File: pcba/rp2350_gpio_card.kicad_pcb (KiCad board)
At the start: 2 copper layers, 26 x 30 mm, 41 parts, among them J1 Conn_01x10_Pin, J2 Conn_01x10_Pin, P1 USB_C_Plug_USB2.0, U1 RP2350_60QFN, U2 W25Q128JVS, U4 AP2127K-3.3, Y1 ABM8-272-T3

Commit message: add copyright claim
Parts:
- moved C1 3.78 mm to (92.7, 65.0)
- moved C13 3.78 mm to (112.5, 75.7)
- moved C15 3.78 mm to (114.2, 58.0)
- moved C3 3.78 mm to (95.3, 64.5)
- moved R4 3.78 mm to (99.7, 57.5)
- moved R6 3.78 mm to (102.0, 72.5)
- moved R8 3.78 mm to (112.5, 64.9)
- moved Y1 3.78 mm to (113.1, 61.6)
- moved C10 3.78 mm to (108.6, 61.6)
- moved C12 3.78 mm to (114.1, 68.0)
- moved C14 3.78 mm to (103.6, 60.0)
- moved C16 3.78 mm to (113.9, 64.0)
- moved C17 3.78 mm to (97.8, 66.1)
- moved C19 3.78 mm to (94.1, 54.1)
- moved C2 3.78 mm to (110.8, 56.7)
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
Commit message: update design
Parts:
- J1, J2: footprint Connector_Harwin:Harwin_M20-89010xx_1x10_P2.54mm_Horizontal -> RP2350CardCustomFootprintsLibrary:Custom_Harwin_M20-89010xx_1x10_P2.54mm_Horizontal
- moved REF** 11.4 mm to (112.6, 56.0)
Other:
- board text added: "EE student at Polytechnic University of Turin"

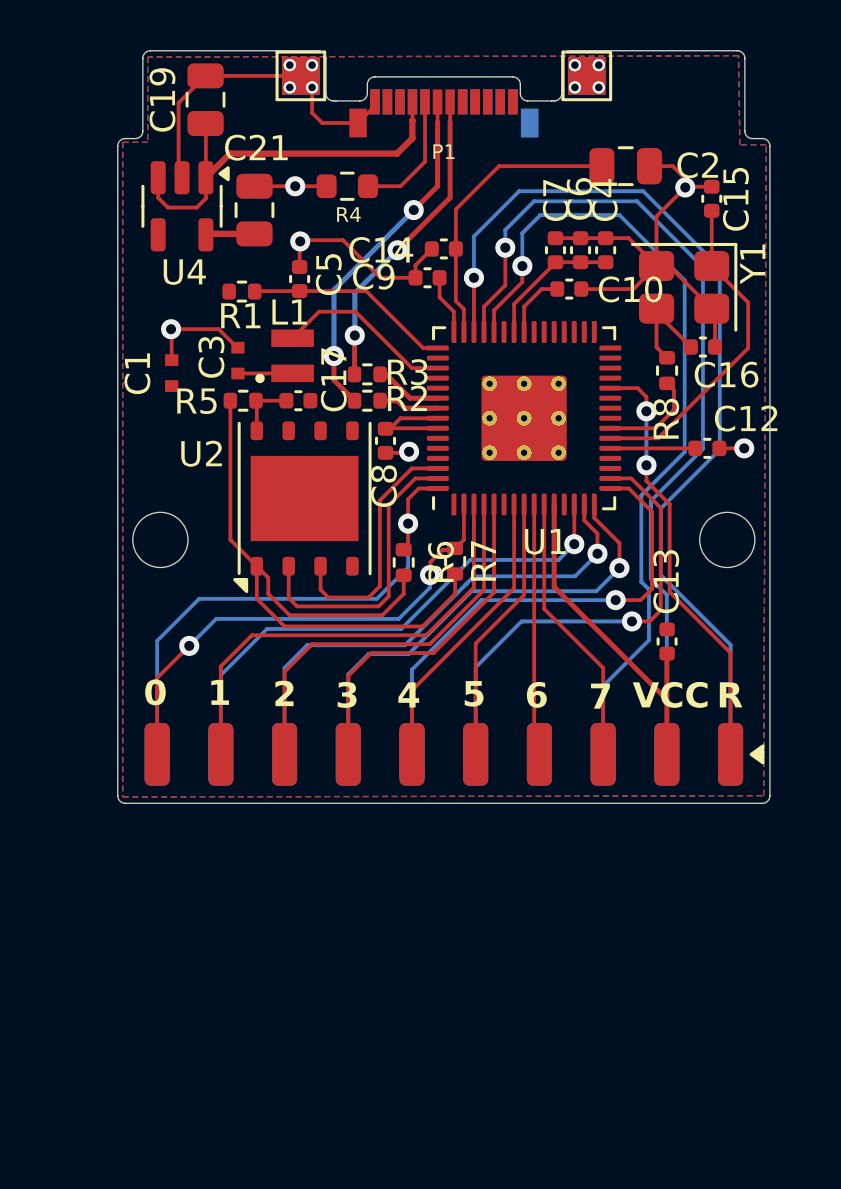
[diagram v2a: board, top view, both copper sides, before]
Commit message: version 1.2.4 - fix floating pads and some errors
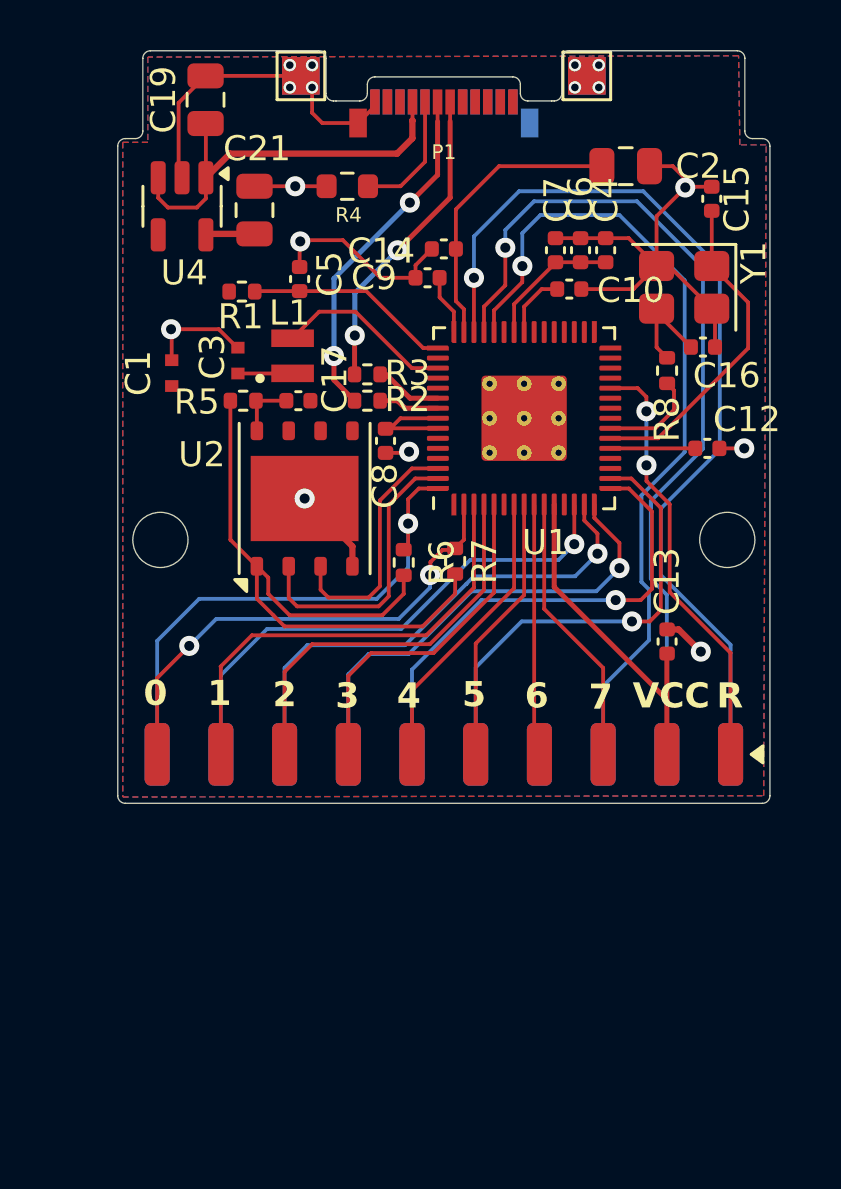
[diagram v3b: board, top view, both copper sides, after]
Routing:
- net GND: track 48.2 -> 53.4 mm, vias 14 -> 16
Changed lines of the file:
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@@
 	(paper "A5")
 	(title_block
-		(title "RP2350 GPIO Card V1.2.2")
+		(title "RP2350 GPIO Card V1.2.4")
 		(date "2025-08-07")
 		(rev "X1")
@@
 	)
 	(segment
-		(start 103.305183 57.546434)
+		(start 103.305183 57.094817)
 		(end 103.305183 54.971434)
 		(width 0.2)
@@
 	)
 	(segment
-		(start 102.355183 58.496434)
-		(end 103.305183 57.546434)
+		(start 102.2 58.2)
+		(end 103.305183 57.094817)
 		(width 0.2)
 		(layer "F.Cu")
@@
 	)
 	(via
-		(at 102.355183 58.496434)
+		(at 102.2 58.2)
 		(size 0.8)
 		(drill 0.4)
@@
 	)
 	(segment
-		(start 99.174254 61.677363)
-		(end 102.355183 58.496434)
+		(start 99.174254 61.225746)
+		(end 99.174254 64.31513)
 		(width 0.2)
 		(layer "B.Cu")
@@
 	)
 	(segment
-		(start 99.174254 64.31513)
-		(end 99.174254 61.677363)
+		(start 102.2 58.2)
+		(end 99.174254 61.225746)
 		(width 0.2)
 		(layer "B.Cu")
@@
 	)
 	(segment
+		(start 99.910183 72.696434)
+		(end 99.910183 71.901434)
+		(width 0.25)
+		(layer "F.Cu")
+		(net 55)
+	)
+	(segment
 		(start 95.315183 63.981434)
 		(end 94.580183 63.246434)
@@
 	)
 	(segment
+		(start 99.910183 71.901434)
+		(end 98.005183 69.996434)
+		(width 0.25)
+		(layer "F.Cu")
+		(net 55)
+	)
+	(segment
 		(start 94.580183 63.246434)
 		(end 92.680183 63.246434)
@@
 	)
 	(segment
+		(start 112.916434 75.216434)
+		(end 113.8 76.1)
+		(width 0.25)
+		(layer "F.Cu")
+		(net 55)
+	)
+	(segment
 		(start 114.365183 62.556434)
 		(end 114.235183 62.426434)
@@
 	)
 	(segment
+		(start 112.455183 75.216434)
+		(end 112.916434 75.216434)
+		(width 0.25)
+		(layer "F.Cu")
+		(net 55)
+	)
+	(segment
 		(start 112.535183 60.726434)
 		(end 112.035183 60.726434)
@@
 	)
 	(via
+		(at 98.005183 69.996434)
+		(size 0.8)
+		(drill 0.4)
+		(layers "F.Cu" "B.Cu")
+		(net 55)
+	)
+	(via
 		(at 92.680183 63.246434)
 		(size 0.8)
@@
 		(layers "F.Cu" "B.Cu")
 		(net 55)
+	)
+	(via
+		(at 113.8 76.1)
+		(size 0.8)
+		(drill 0.4)
+		(layers "F.Cu" "B.Cu")
+		(net 55)

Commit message: version 1.3.0 - major fixes for floating pins
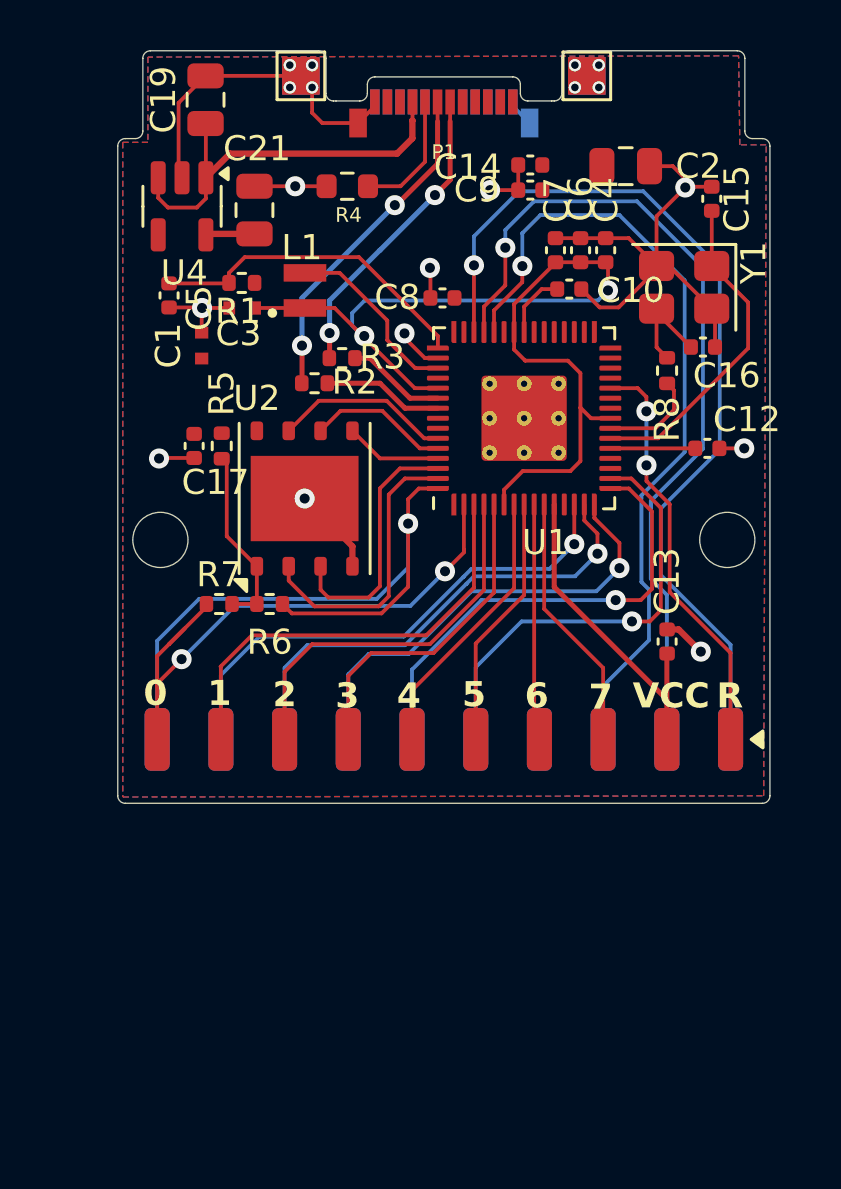
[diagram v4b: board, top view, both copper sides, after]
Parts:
- moved R7 9.56 mm to (94.6, 74.2), turned to 0 degrees
- moved C8 6.13 mm to (103.5, 62.0), turned to 180 degrees
- moved R6 5.60 mm to (96.6, 74.2), turned to 180 degrees
- moved C9 5.38 mm to (107.0, 57.7)
- moved C5 5.25 mm to (92.6, 61.9), turned to -90 degrees
- moved C14 4.80 mm to (107.0, 56.7)
- moved C17 4.53 mm to (93.6, 67.9), turned to -90 degrees
- moved L1 2.65 mm to (98.0, 61.7)
- moved R2 2.22 mm to (98.4, 65.4)
- moved C3 2.10 mm to (95.5, 62.4), turned to 180 degrees
- moved R5 2.00 mm to (94.7, 67.9), turned to -90 degrees
- moved C1 1.62 mm to (93.9, 63.9)
- moved R3 1.20 mm to (99.5, 64.4)
- moved J1 0.60 mm to (103.6, 85.1)
- moved J2 0.60 mm to (103.6, 85.1)
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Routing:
- net +1V1: track 7.72 -> 39.9 mm, vias 0 -> 2
- net +3.3V: track 42.0 -> 21.7 mm
- net /FLASH_SS: track 26.2 -> 7.37 mm
- net /QSPI_SD3: track 0.00 -> 7.06 mm
- net /QSPI_SS: track 20.9 -> 28.0 mm
- net /QSPI_SCLK: track 0.00 -> 5.63 mm
- net /VREG_AVDD: track 8.25 -> 13.2 mm
- net /GPIO0: track 19.5 -> 23.5 mm
- net /QSPI_SD0: track 0.00 -> 3.86 mm
- net Net-(U1-USB_DP): track 2.43 -> 4.82 mm
- net Net-(U1-USB_DM): track 2.70 -> 3.98 mm
- net GND: track 53.4 -> 52.4 mm, vias 16 -> 18

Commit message: version 1.3.1 - thermal fix, new render
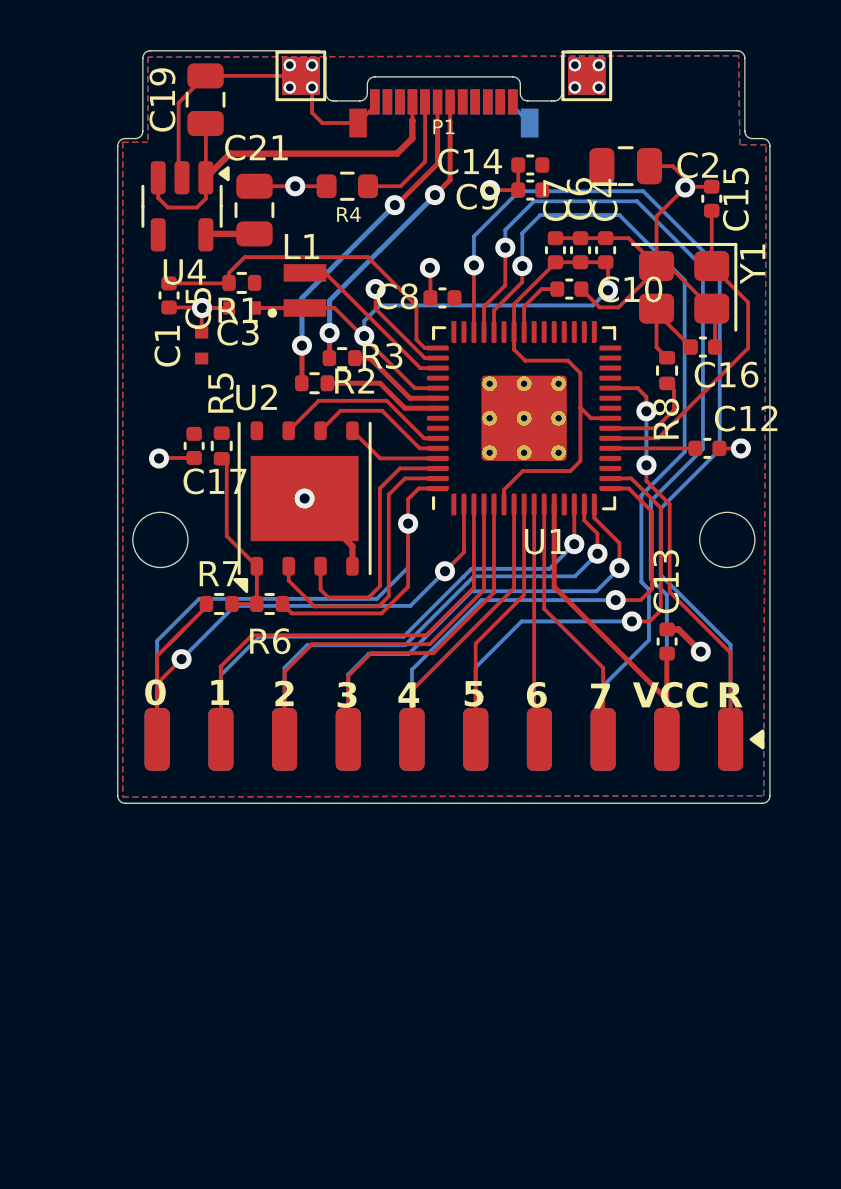
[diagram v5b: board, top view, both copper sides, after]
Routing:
- net GND: track 52.4 -> 54.5 mm
- net +1V1: track 39.9 -> 39.0 mm
- net /VREG_AVDD: track 13.2 -> 13.7 mm
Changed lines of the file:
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@@
 	(paper "A5")
 	(title_block
-		(title "RP2350 GPIO Card V1.3.0")
-		(date "2025-08-07")
+		(title "RP2350 GPIO Card V1.3.1")
+		(date "2025-08-24")
 		(rev "X1")
 		(company "SemiTO-V Student Team, Polytechnic University of Turin")
@@
 		(tags "USB Type-C Plug Edge Mount")
 		(property "Reference" "P1"
-			(at 0 2.04 0)
+			(at 0 1.053566 0)
 			(layer "F.SilkS")
 			(effects
@@
 		(tags "capacitor")
 		(property "Reference" "C9"
-			(at 2.135 0.01 0)
+			(at 2.1 -0.3 0)
 			(layer "F.SilkS")
 			(effects
@@
 		(tags "capacitor")
 		(property "Reference" "C14"
-			(at 2.495 -0.08 0)
+			(at 2.4 0.1 0)
 			(layer "F.SilkS")
 			(effects
@@
 	)
 	(segment
-		(start 100.382403 63.516978)
-		(end 100.316978 63.516978)
+		(start 101 62.3)
+		(end 109.5 62.3)
 		(width 0.1524)
 		(layer "B.Cu")
@@
 	)
 	(segment
-		(start 99.9 62.6)
-		(end 100.4 62.1)
-		(width 0.1524)
-		(layer "B.Cu")
-		(net 1)
-	)
-	(segment
-		(start 100.316978 63.516978)
-		(end 99.9 63.1)
+		(start 109.5 62.3)
+		(end 110.1 61.7)
 		(width 0.1524)
 		(layer "B.Cu")
@@
 	)
 	(segment
-		(start 100.4 62.1)
-		(end 109.7 62.1)
+		(start 100.382403 63.516978)
+		(end 100.316978 63.516978)
 		(width 0.1524)
 		(layer "B.Cu")
@@
 	)
 	(segment
-		(start 109.7 62.1)
-		(end 110.1 61.7)
+		(start 100.382403 63.516978)
+		(end 100.382403 62.917597)
 		(width 0.1524)
 		(layer "B.Cu")
@@
 	)
 	(segment
-		(start 99.9 63.1)
-		(end 99.9 62.6)
+		(start 100.382403 62.917597)
+		(end 101 62.3)
 		(width 0.1524)
 		(layer "B.Cu")
@@
 	)
 	(segment
-		(start 100.1728 60.3728)
-		(end 103.317683 63.517683)
+		(start 102.4628 62.313086)
+		(end 102.4628 63.6628)
 		(width 0.1524)
 		(layer "F.Cu")
@@
 	)
 	(segment
-		(start 103.317683 63.517683)
-		(end 103.317683 63.996434)
+		(start 100.522514 60.3728)
+		(end 102.4628 62.313086)
 		(width 0.1524)
 		(layer "F.Cu")
@@
 	)
 	(segment
-		(start 92.6 61.42)
-		(end 94.97 61.42)
+		(start 95.6172 60.3728)
+		(end 100.522514 60.3728)
 		(width 0.1524)
 		(layer "F.Cu")
@@
 	)
 	(segment
-		(start 103.314117 64)
-		(end 103.317683 63.996434)
+		(start 102.4628 63.6628)
+		(end 102.796434 63.996434)
 		(width 0.1524)
 		(layer "F.Cu")
@@
 	)
 	(segment
-		(start 95.6172 60.3728)
-		(end 100.1728 60.3728)
+		(start 94.99 61.4)
+		(end 94.99 61)
 		(width 0.1524)
 		(layer "F.Cu")
@@
 	)
 	(segment
-		(start 94.99 61.4)
-		(end 94.99 61)
+		(start 92.6 61.42)
+		(end 94.97 61.42)
+		(width 0.1524)
+		(layer "F.Cu")
+		(net 3)
+	)
+	(segment
+		(start 102.796434 63.996434)
+		(end 103.317683 63.996434)
+		(width 0.1524)
+		(layer "F.Cu")
+		(net 3)
+	)
+	(segment
+		(start 103.314117 64)
+		(end 103.317683 63.996434)
 		(width 0.1524)
 		(layer "F.Cu")
@@
 	)
 	(segment
-		(start 101.3 62.9)
-		(end 99.4 61)
-		(width 0.1524)
-		(layer "F.Cu")
-		(net 25)
-	)
-	(segment
-		(start 99.4 61)
-		(end 98.018156 61)
+		(start 102.619565 64.796434)
+		(end 98.823131 61)
 		(width 0.1524)
 		(layer "F.Cu")
@@
 	(segment
 		(start 103.317683 64.796434)
-		(end 102.412612 64.796434)
-		(width 0.1524)
-		(layer "F.Cu")
-		(net 25)
-	)
-	(segment
-		(start 101.3 63.683822)
-		(end 101.3 62.9)
+		(end 102.619565 64.796434)
 		(width 0.1524)
 		(layer "F.Cu")
@@
 	)
 	(segment
-		(start 102.412612 64.796434)
-		(end 101.3 63.683822)
+		(start 98.823131 61)
+		(end 98.018156 61)
 		(width 0.1524)
 		(layer "F.Cu")
@@
 	)
 	(segment
-		(start 102.796434 64.396434)
-		(end 103.317683 64.396434)
+		(start 96.005183 57.546434)
+		(end 97.630183 57.546434)
 		(width 0.1524)
 		(layer "F.Cu")
@@
 	)
 	(segment
-		(start 96.005183 57.546434)
-		(end 97.630183 57.546434)
+		(start 115.4 68)
+		(end 114.543749 68)
 		(width 0.1524)
 		(layer "F.Cu")
@@
 	)
 	(segment
+		(start 102.796434 64.396434)
+		(end 103.317683 64.396434)
+		(width 0.1524)
+		(layer "F.Cu")
+		(net 55)
+	)
+	(segment
 		(start 109.765949 62.3772)
 		(end 110.5228 62.3772)
@@
 	)
 	(segment
+		(start 102.796434 64.396434)
+		(end 100.835997 62.435997)
+		(width 0.1524)
+		(layer "F.Cu")
+		(net 55)
+	)
+	(segment
 		(start 110.5228 62.3772)
 		(end 112.035183 60.864817)
@@
 	)
 	(segment
+		(start 114.543749 68)
+		(end 114.540183 67.996434)
+		(width 0.1524)
+		(layer "F.Cu")
+		(net 55)
+	)
+	(segment
 		(start 112.535183 60.726434)
 		(end 112.035183 60.726434)
@@
 	)
 	(segment
-		(start 101.986235 63.586235)
-		(end 102.796434 64.396434)
-		(width 0.1524)
-		(layer "F.Cu")
-		(net 55)
-	)
-	(segment
 		(start 92.22 68.38)
 		(end 92.2 68.4)
@@
 	)
 	(segment
-		(start 114.235183 57.566434)
-		(end 113.210183 57.566434)
+		(start 100.835997 62.435997)
+		(end 100.835997 61.643989)
 		(width 0.1524)
 		(layer "F.Cu")
@@
 	)
 	(segment
-		(start 101.986235 63.413765)
-		(end 101.986235 63.586235)
+		(start 114.235183 57.566434)
+		(end 113.210183 57.566434)
 		(width 0.1524)
 		(layer "F.Cu")
@@
 	)
 	(segment
-		(start 114.540183 67.996434)
-		(end 115.530183 67.996434)
-		(width 0.1524)
-		(layer "F.Cu")
-		(net 55)
-	)
-	(segment
 		(start 92.980183 54.221434)
 		(end 94.055183 53.146434)
@@
 	)
 	(via
-		(at 115.530183 67.996434)
+		(at 115.4 68)
 		(size 0.8)
 		(drill 0.4)
@@
 	)
 	(via
-		(at 101.986235 63.413765)
-		(size 0.8)
-		(drill 0.4)
-		(layers "F.Cu" "B.Cu")
-		(net 55)
-	)
-	(via
 		(at 108.779683 53.606934)
 		(size 0.5)
@@
 		(size 0.8)
 		(drill 0.4)
+		(layers "F.Cu" "B.Cu")
+		(net 55)
+	)
+	(via
+		(at 100.835997 61.643989)
+		(size 0.8)
+		(drill 0.4)
